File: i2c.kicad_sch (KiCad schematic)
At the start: 4 parts, among them J14 Conn_02x03_Top_Bottom, U9 LTC4311

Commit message: sch, pcb: update pn fields
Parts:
- C9: value 100nF -> 100nF 16v; Part Number (none) -> GRM155R71C104KA88D
- J14: Part Number (none) -> 1053101106
- U9: Part Number (none) -> LTC4311CSC6#TRPBF
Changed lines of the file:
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@@
+			)
+		)
+		(property "Part Number" "1053101106"
+			(at 181.61 97.79 0)
+			(effects
+				(font
+					(size 1.27 1.27)
+				)
+				(hide yes)
 			)
 		)
@@
 			)
 		)
-		(property "Value" "100nF"
-			(at 143.51 71.12 0)
+		(property "Value" "100nF 16v"
+			(at 143.51 63.754 0)
 			(effects
 				(font
@@
 		)
 		(property "Description" "Unpolarized capacitor"
+			(at 144.78 80.01 0)
+			(effects
+				(font
+					(size 1.27 1.27)
+				)
+				(hide yes)
+			)
+		)
+		(property "Part Number" "GRM155R71C104KA88D"
 			(at 144.78 80.01 0)
 			(effects
@@
 			(at 144.78 97.79 0)
 			(effects
+				(font
+					(size 1.27 1.27)
+				)
+				(hide yes)
+			)
+		)
+		(property "Part Number" "LTC4311CSC6#TRPBF"
+			(at 144.78 97.79 0)
+			(effects

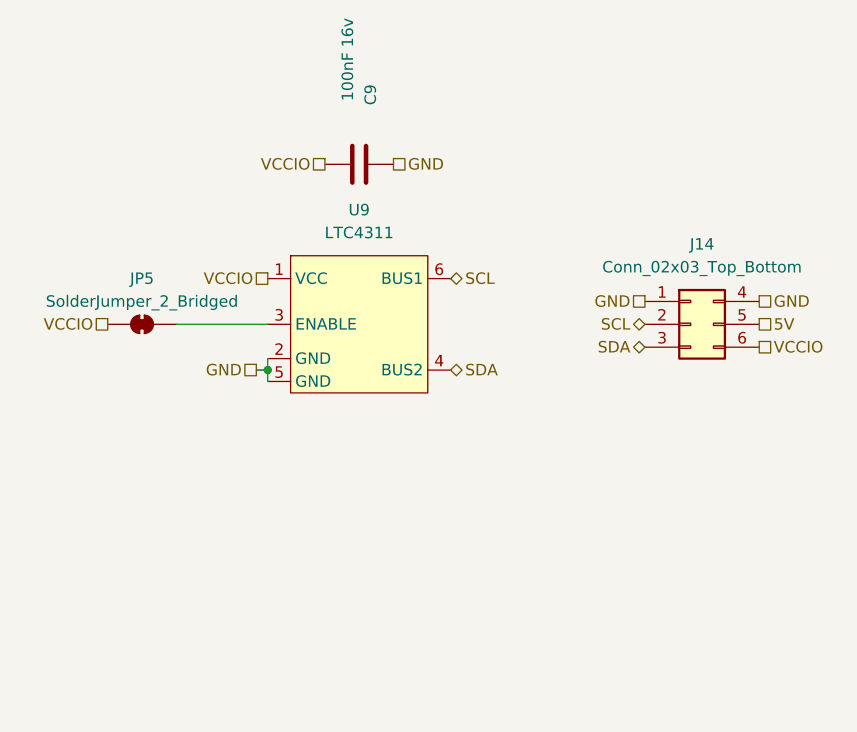
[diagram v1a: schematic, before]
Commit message: i2c, servo, pcb: pca9685 servo, pcb, rs422: leds
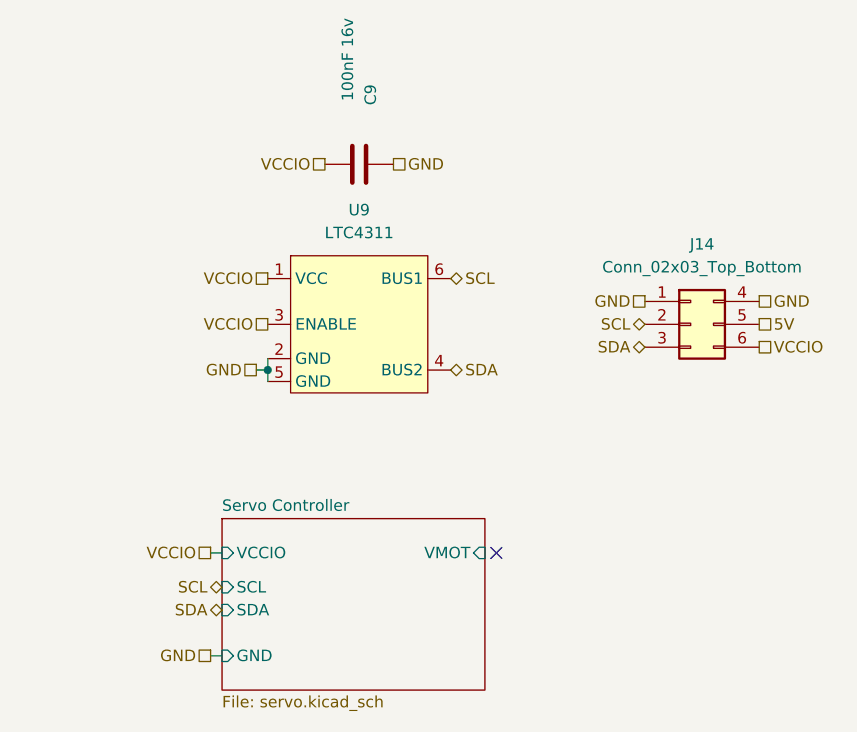
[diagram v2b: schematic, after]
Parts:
- removed JP5: SolderJumper_2_Bridged, Jumper:SolderJumper-2_P1.3mm_Bridged_RoundedPad1.0x1.5mm, symbol Jumper:SolderJumper_2_Bridged
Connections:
- net VCCIO: now also U9.3 (ENABLE)
- no-connect marks 0 -> 1
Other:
- added sheet Servo Controller (servo.kicad_sch)
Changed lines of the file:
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@@
 		(color 0 0 0 0)
+	)
+	(no_connect
+		(at 160.02 123.19)
 	)
 	(wire
 		(pts
-			(xy 124.46 97.79) (xy 134.62 97.79)
+			(xy 128.27 123.19) (xy 129.54 123.19)
 		)
 		(stroke
@@
 	(wire
 		(pts
-			(xy 134.62 101.6) (xy 134.62 102.87)
+			(xy 128.27 134.62) (xy 129.54 134.62)
 		)
 		(stroke
@@
 	(wire
 		(pts
-			(xy 134.62 102.87) (xy 134.62 104.14)
+			(xy 134.62 101.6) (xy 134.62 102.87)
 		)
 		(stroke
@@
 		)
 	)
+	(wire
+		(pts
+			(xy 134.62 102.87) (xy 134.62 104.14)
+		)
+		(stroke
+			(width 0)
+			(type default)
+		)
+	)
 	(hierarchical_label "SDA"
 		(shape bidirectional)
@@
 	(hierarchical_label "VCCIO"
 		(shape passive)
-		(at 116.84 97.79 180)
+		(at 134.62 97.79 180)
 		(effects
 			(font
@@
 		)
 	)
+	(hierarchical_label "GND"
+		(shape passive)
+		(at 128.27 134.62 180)
+		(effects
+			(font
+				(size 1.27 1.27)
+			)
+			(justify right)
+		)
+	)
 	(hierarchical_label "5V"
 		(shape passive)
@@
 	(hierarchical_label "VCCIO"
 		(shape passive)
+		(at 128.27 123.19 180)
+		(effects
+			(font
+				(size 1.27 1.27)
+			)
+			(justify right)
+		)
+	)
+	(hierarchical_label "VCCIO"
+		(shape passive)
 		(at 134.62 92.71 180)
 		(effects
@@
 			)
 			(justify left)
+		)
+	)
+	(hierarchical_label "SDA"
+		(shape bidirectional)
+		(at 129.54 129.54 180)
+		(effects
+			(font
+				(size 1.27 1.27)
+			)
+			(justify right)
+		)
+	)
+	(hierarchical_label "SCL"
+		(shape bidirectional)
+		(at 129.54 127 180)
+		(effects
+			(font
+				(size 1.27 1.27)
+			)
+			(justify right)
 		)
 	)
@@
 			)
 			(justify right)
-		)
-	)
-	(symbol
-		(lib_id "Jumper:SolderJumper_2_Bridged")
-		(at 120.65 97.79 0)
-		(unit 1)
-		(exclude_from_sim no)
-		(in_bom no)
-		(on_board yes)
-		(dnp no)
-		(property "Reference" "JP5"
-			(at 120.65 92.71 0)
-			(effects
-				(font
-					(size 1.27 1.27)
-				)
-			)
-		)
-		(property "Value" "SolderJumper_2_Bridged"
-			(at 120.65 95.25 0)
-			(effects
-				(font
-					(size 1.27 1.27)
-				)
-			)
-		)
-		(property "Footprint" "Jumper:SolderJumper-2_P1.3mm_Bridged_RoundedPad1.0x1.5mm"
-			(at 120.65 97.79 0)
-			(effects
-				(font
-					(size 1.27 1.27)
-				)
-				(hide yes)
-			)
-		)
-		(property "Datasheet" "~"
-			(at 120.65 97.79 0)
-			(effects
-				(font
-					(size 1.27 1.27)
-				)
-				(hide yes)
-			)
-		)
-		(property "Description" "Solder Jumper, 2-pole, closed/bridged"
-			(at 120.65 97.79 0)
-			(effects
-				(font
-					(size 1.27 1.27)
-				)
-				(hide yes)
-			)
-		)
-		(pin "2"
-		)
-		(pin "1"
-		)
-		(instances
-			(project ""
-				(path "/362ca48c-0b77-4943-b8b3-fc15ab97f30d/7b0b1465-76e8-4550-9366-259d540e6b80"
-					(reference "JP5")
-					(unit 1)
-				)
-			)
 		)
 	)
@@
 				)
 			)
+		)
+	)
+	(sheet
+		(at 129.54 119.38)
+		(size 29.21 19.05)
+		(exclude_from_sim no)
+		(in_bom yes)
+		(on_board yes)
+		(dnp no)
+		(fields_autoplaced yes)
+		(stroke
+			(width 0.1524)
+			(type solid)
+		)
+		(fill
+			(color 0 0 0 0.0000)
+		)
+		(property "Sheetname" "Servo Controller"
+			(at 129.54 118.6684 0)
+			(effects
+				(font
+					(size 1.27 1.27)
+				)
+				(justify left bottom)
+			)
+		)
+		(property "Sheetfile" "servo.kicad_sch"
+			(at 129.54 139.0146 0)
+			(effects
+				(font
+					(size 1.27 1.27)
+				)
+				(justify left top)
+			)
+		)
+		(pin "GND" input
+			(at 129.54 134.62 180)
+			(effects
+				(font
+					(size 1.27 1.27)
+				)
+				(justify left)
+			)
+		)
+		(pin "VMOT" input
+			(at 158.75 123.19 0)
+			(effects
+				(font
+					(size 1.27 1.27)
+				)
+				(justify right)
+			)
+		)
+		(pin "SCL" input
+			(at 129.54 127 180)
+			(effects
+				(font
+					(size 1.27 1.27)
+				)
+				(justify left)
+			)
+		)
+		(pin "SDA" input
+			(at 129.54 129.54 180)
+			(effects
+				(font
+					(size 1.27 1.27)
+				)
+				(justify left)
+			)
+		)
+		(pin "VCCIO" input
+			(at 129.54 123.19 180)
+			(effects
+				(font
+					(size 1.27 1.27)
+				)
+				(justify left)
+			)
+		)
+		(instances
+			(project "P2 Kevinbot Board"
+				(path "/362ca48c-0b77-4943-b8b3-fc15ab97f30d/7b0b1465-76e8-4550-9366-259d540e6b80"
+					(page "10")
+				)
+			)

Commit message: sch: erc
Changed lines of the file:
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@@
 	)
 	(no_connect
-		(at 160.02 123.19)
+		(at 158.75 123.19)
 	)
 	(wire
